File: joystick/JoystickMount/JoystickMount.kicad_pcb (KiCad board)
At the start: 2 copper layers, 2 parts

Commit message: update joystick mount
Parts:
- JOYSTICK_J1: footprint ErgoCai.pretty:CONN-TH_S5B-ZR-LF-SN -> ErgoCai.pretty:FPC-SMD_AFC01-S05FCA-00
- moved JOYSTICK_J1 3.71 mm to (-1.28, 0.00)

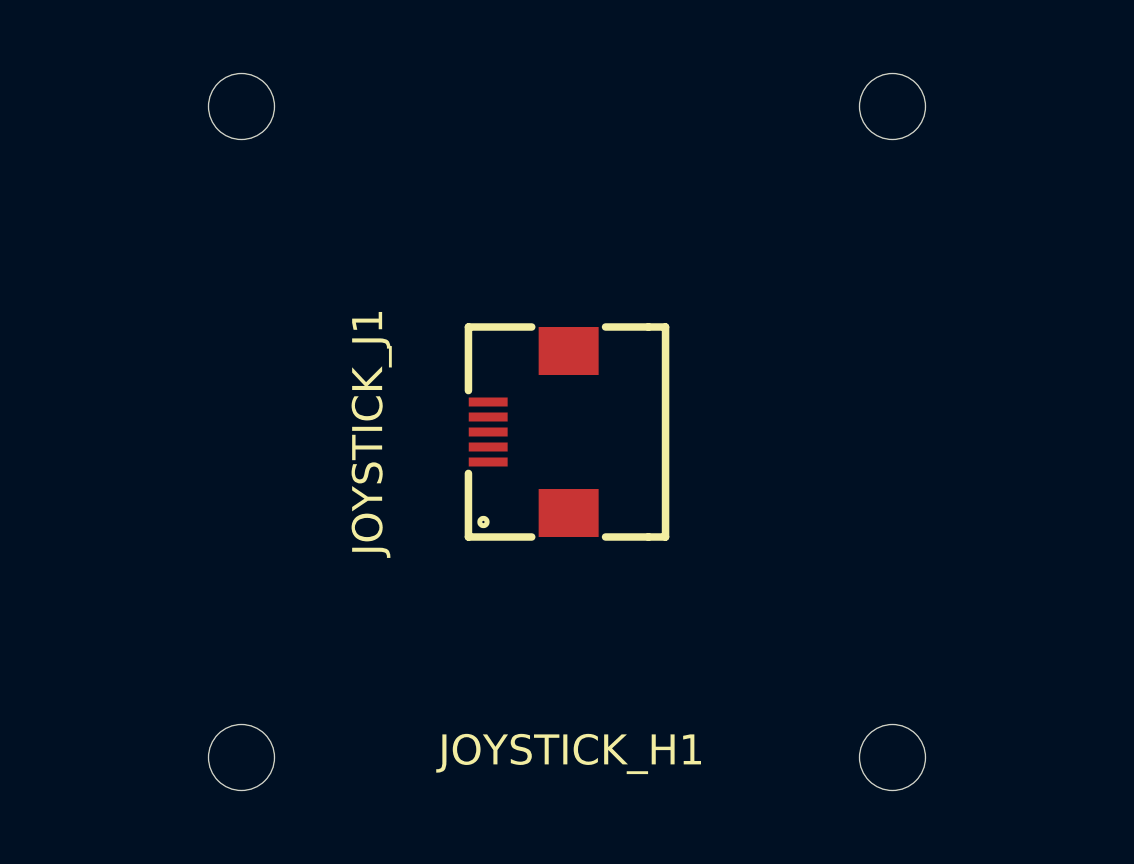
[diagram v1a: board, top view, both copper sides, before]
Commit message: update joystick size
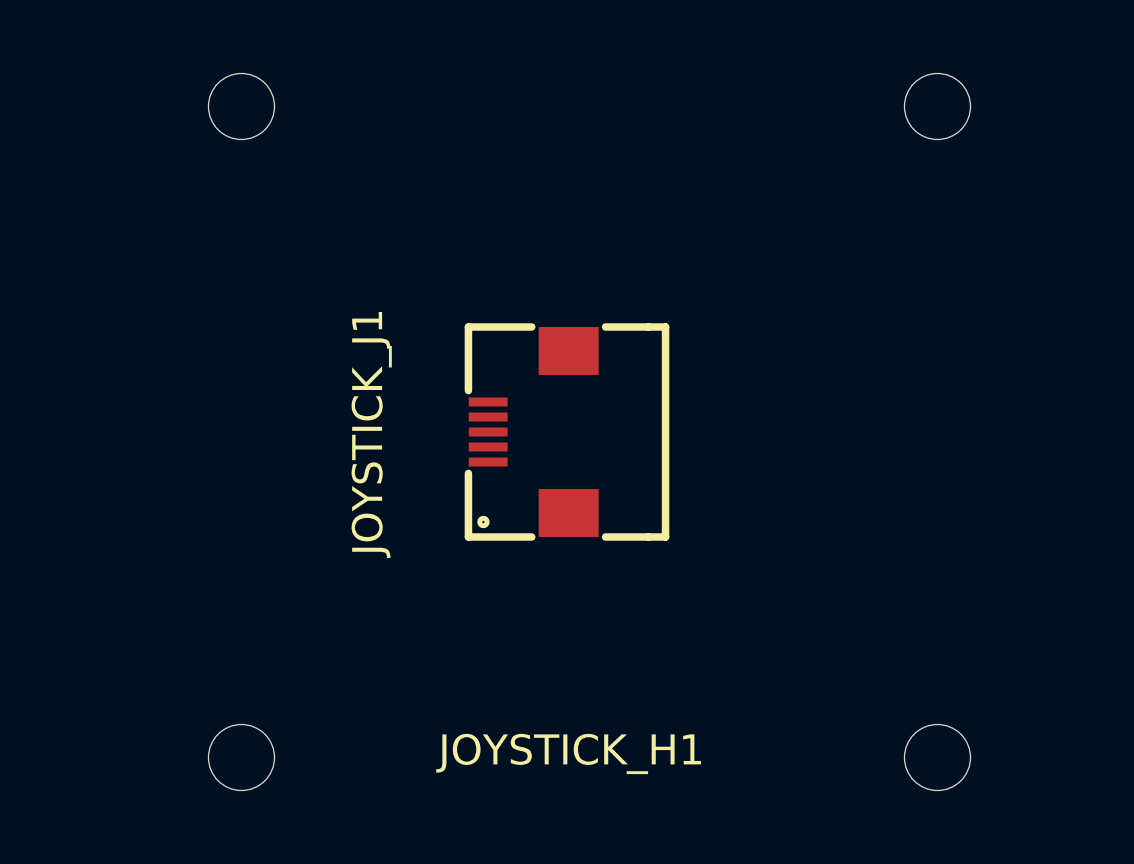
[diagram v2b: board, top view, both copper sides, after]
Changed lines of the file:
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@@
 		(fp_rect
 			(start -13 -13)
-			(end 13 13)
+			(end 14.5 13)
 			(stroke
 				(width 0.1)
@@
 		)
 		(fp_circle
-			(center 10.85 -10.85)
-			(end 12.75 -10.85)
+			(center 12.35 -10.85)
+			(end 14.25 -10.85)
 			(stroke
 				(width 0.15)
@@
 		)
 		(fp_circle
-			(center 10.85 10.85)
-			(end 12.75 10.85)
+			(center 12.35 10.85)
+			(end 14.25 10.85)
 			(stroke
 				(width 0.15)
@@
 		)
 		(fp_circle
-			(center 10.85 -10.85)
-			(end 13 -10.85)
+			(center 12.35 -10.85)
+			(end 14.5 -10.85)
 			(stroke
 				(width 0.05)
@@
 		)
 		(fp_circle
-			(center 10.85 10.85)
-			(end 13 10.85)
+			(center 12.35 10.85)
+			(end 14.5 10.85)
 			(stroke
 				(width 0.05)
@@
 		)
 		(pad "" np_thru_hole circle
-			(at 10.85 -10.85)
+			(at 12.35 -10.85)
 			(size 2.2 2.2)
 			(drill 2.2)
@@
 		)
 		(pad "" np_thru_hole circle
-			(at 10.85 10.85)
+			(at 12.35 10.85)
 			(size 2.2 2.2)
 			(drill 2.2)
@@
 		)
 		(embedded_fonts no)
+		(model "/Users/jinsongc/Development/ErgoCai.modules/joystick/Alpsalpine/Alpsalpine.step"
+			(opacity 0.8100)
+			(offset
+				(xyz 0 0 3.5)
+			)
+			(scale
+				(xyz 1 1 1)
+			)
+			(rotate
+				(xyz -0 -0 -90)
+			)
+		)
+		(model "/Users/jinsongc/Development/ErgoCaiLib/3dmodels/Joystick Cap.stp"
+			(opacity 0.7600)
+			(offset
+				(xyz 0 2.5 23.5)
+			)
+			(scale
+				(xyz 1 1 1)
+			)
+			(rotate
+				(xyz -0 180 90)
+			)
+		)
 	)
 	(embedded_fonts no)

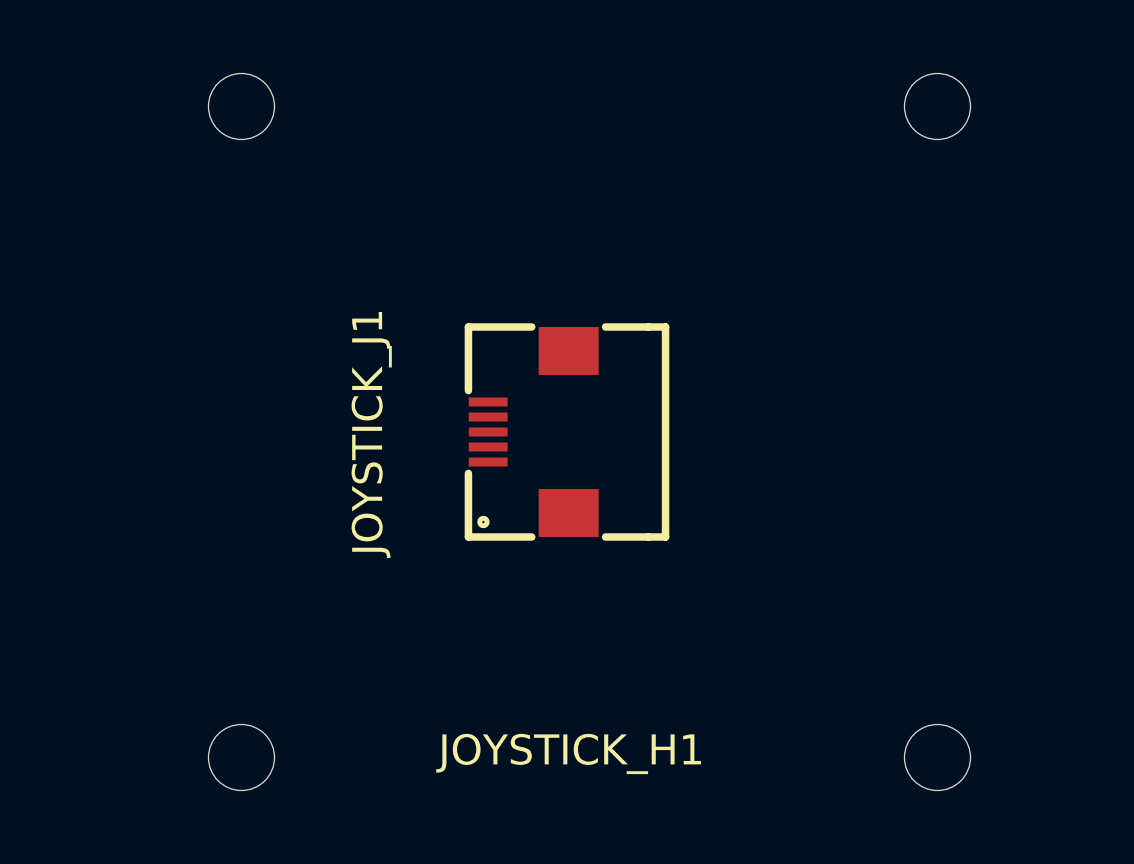
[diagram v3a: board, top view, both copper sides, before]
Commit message: update joystick FPC to 6 pins
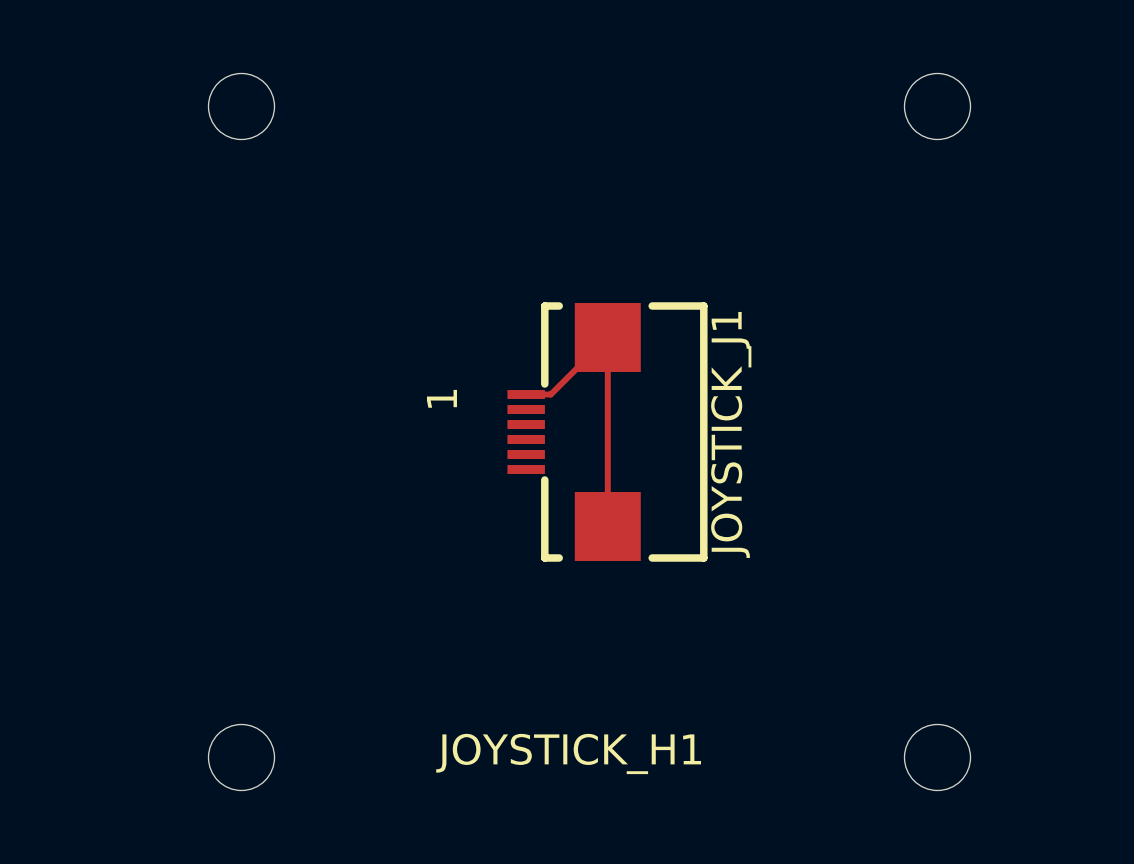
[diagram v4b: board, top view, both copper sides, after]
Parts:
- JOYSTICK_J1: value Conn_01x05 -> AFD01-S06FCA-00; footprint ErgoCai.pretty:FPC-SMD_AFC01-S05FCA-00 -> ErgoCai.pretty:FPC-SMD_6P-P0.50_JS_AFD01-S06FCA-00
- moved JOYSTICK_J1 1.28 mm to (0.00, 0.00), turned to -90 degrees
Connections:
- JOYSTICK_J1 pad 6: (no net) -> unconnected-(JOYSTICK_J1-Pad6)
- JOYSTICK_J1 pad 7: (no net) -> GND
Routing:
- net GND: track 0.00 -> 9.81 mm
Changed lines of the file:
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@@
 	(net 4 "ADC_JT1")
 	(net 5 "ADC_JT2")
-	(footprint "ErgoCai.pretty:FPC-SMD_AFC01-S05FCA-00"
+	(net 6 "unconnected-(JOYSTICK_J1-Pad6)")
+	(footprint "ErgoCai.pretty:FPC-SMD_6P-P0.50_JS_AFD01-S06FCA-00"
 		(layer "F.Cu")
-		(at -1.285 0 90)
+		(at 0 0 -90)
 		(property "Reference" "JOYSTICK_J1"
-			(at 0 -5.34 90)
-			(layer "F.SilkS")
-			(effects
-				(font
-					(size 1 1)
-					(thickness 0.15)
-				)
-			)
-		)
-		(property "Value" "Conn_01x05"
-			(at 0 5.34 90)
-			(layer "F.Fab")
-			(effects
-				(font
-					(size 1 1)
-					(thickness 0.15)
-				)
-			)
-		)
-		(property "Datasheet" "~"
+			(at 0 -5.36 90)
+			(layer "F.SilkS")
+			(effects
+				(font
+					(size 1 1)
+					(thickness 0.15)
+				)
+			)
+		)
+		(property "Value" "AFD01-S06FCA-00"
+			(at 0 5.36 90)
+			(layer "F.Fab")
+			(effects
+				(font
+					(size 1 1)
+					(thickness 0.15)
+				)
+			)
+		)
+		(property "Datasheet" ""
 			(at 0 0 90)
 			(layer "F.Fab")
@@
 			)
 		)
-		(property "Description" "Generic connector, single row, 01x05, script generated (kicad-library-utils/schlib/autogen/connector/)"
+		(property "Description" ""
 			(at 0 0 90)
 			(layer "F.Fab")
@@
 			)
 		)
-		(property ki_fp_filters "Connector*:*_1x??_*")
+		(property "LCSC Part" "C18198574"
+			(at 0 0 270)
+			(unlocked yes)
+			(layer "F.Fab")
+			(hide yes)
+			(effects
+				(font
+					(size 1 1)
+					(thickness 0.15)
+				)
+			)
+		)
 		(sheetname "/")
 		(sheetfile "JoystickMount.kicad_sch")
-		(attr smd)
-		(fp_line
-			(start 3.5 -2)
-			(end 3.5 0.11)
-			(stroke
-				(width 0.25)
-				(type solid)
-			)
-			(layer "F.SilkS")
-		)
-		(fp_line
-			(start 1.38 -2)
-			(end 3.5 -2)
-			(stroke
-				(width 0.25)
-				(type solid)
-			)
-			(layer "F.SilkS")
-		)
-		(fp_line
-			(start -3.5 -2)
-			(end -1.38 -2)
-			(stroke
-				(width 0.25)
-				(type solid)
-			)
-			(layer "F.SilkS")
-		)
-		(fp_line
-			(start -3.5 -2)
-			(end -3.5 0.11)
-			(stroke
-				(width 0.25)
-				(type solid)
-			)
-			(layer "F.SilkS")
-		)
-		(fp_line
-			(start 3.5 2.57)
-			(end 3.5 4)
-			(stroke
-				(width 0.25)
-				(type solid)
-			)
-			(layer "F.SilkS")
-		)
-		(fp_line
-			(start -3.5 2.57)
-			(end -3.5 4)
-			(stroke
-				(width 0.25)
-				(type solid)
-			)
-			(layer "F.SilkS")
-		)
-		(fp_line
-			(start 3.5 4)
-			(end 3.5 4.57)
-			(stroke
-				(width 0.25)
-				(type solid)
-			)
-			(layer "F.SilkS")
-		)
-		(fp_line
-			(start -3.5 4)
-			(end -3.5 4.57)
-			(stroke
-				(width 0.25)
-				(type solid)
-			)
-			(layer "F.SilkS")
-		)
-		(fp_line
-			(start 3.5 4.57)
-			(end -3.5 4.57)
-			(stroke
-				(width 0.25)
-				(type solid)
-			)
-			(layer "F.SilkS")
-		)
-		(fp_circle
-			(center -3 -1.5)
-			(end -2.92 -1.5)
-			(stroke
-				(width 0.25)
-				(type solid)
-			)
-			(fill no)
-			(layer "F.SilkS")
-		)
-		(fp_circle
-			(center -3.45 -1.71)
-			(end -3.42 -1.71)
-			(stroke
-				(width 0.06)
-				(type solid)
-			)
-			(fill no)
-			(layer "F.Fab")
+		(attr through_hole)
+		(fp_line
+			(start -4.2 0.74)
+			(end -1.6 0.74)
+			(stroke
+				(width 0.25)
+				(type solid)
+			)
+			(layer "F.SilkS")
+		)
+		(fp_line
+			(start 4.2 0.74)
+			(end 1.6 0.74)
+			(stroke
+				(width 0.25)
+				(type solid)
+			)
+			(layer "F.SilkS")
+		)
+		(fp_line
+			(start -4.2 0.26)
+			(end -4.2 0.74)
+			(stroke
+				(width 0.25)
+				(type solid)
+			)
+			(layer "F.SilkS")
+		)
+		(fp_line
+			(start 4.2 0.26)
+			(end 4.2 0.74)
+			(stroke
+				(width 0.25)
+				(type solid)
+			)
+			(layer "F.SilkS")
+		)
+		(fp_line
+			(start -4.2 -4.56)
+			(end -4.2 -2.84)
+			(stroke
+				(width 0.25)
+				(type solid)
+			)
+			(layer "F.SilkS")
+		)
+		(fp_line
+			(start 4.2 -4.56)
+			(end 4.2 -2.84)
+			(stroke
+				(width 0.25)
+				(type solid)
+			)
+			(layer "F.SilkS")
+		)
+		(fp_line
+			(start 4.2 -4.56)
+			(end -4.2 -4.56)
+			(stroke
+				(width 0.25)
+				(type solid)
+			)
+			(layer "F.SilkS")
+		)
+		(fp_text user "1"
+			(at -1.53 4.13 90)
+			(layer "F.SilkS")
+			(effects
+				(font
+					(size 1 1)
+					(thickness 0.2)
+				)
+				(justify right)
+			)
 		)
 		(fp_text user "${REFERENCE}"
@@
 		)
 		(pad "1" smd rect
-			(at -1 -1.34 90)
-			(size 0.3 1.3)
+			(at -1.25 1.36 270)
+			(size 0.3 1.25)
 			(layers "F.Cu" "F.Mask" "F.Paste")
 			(net 1 "GND")
-			(pinfunction "Pin_1")
-			(pintype "passive")
+			(pinfunction "1")
+			(pintype "unspecified")
 		)
 		(pad "2" smd rect
-			(at -0.5 -1.34 90)
-			(size 0.3 1.3)
+			(at -0.75 1.36 270)
+			(size 0.3 1.25)
 			(layers "F.Cu" "F.Mask" "F.Paste")
 			(net 2 "3.3V")
-			(pinfunction "Pin_2")
-			(pintype "passive")
+			(pinfunction "2")
+			(pintype "unspecified")
 		)
 		(pad "3" smd rect
-			(at 0 -1.34 90)
-			(size 0.3 1.3)
+			(at -0.25 1.36 270)
+			(size 0.3 1.25)
 			(layers "F.Cu" "F.Mask" "F.Paste")
 			(net 3 "ADC_JT3")
-			(pinfunction "Pin_3")
-			(pintype "passive")
+			(pinfunction "3")
+			(pintype "unspecified")
 		)
 		(pad "4" smd rect
-			(at 0.5 -1.34 90)
-			(size 0.3 1.3)
+			(at 0.25 1.36 270)
+			(size 0.3 1.25)
 			(layers "F.Cu" "F.Mask" "F.Paste")
 			(net 5 "ADC_JT2")
-			(pinfunction "Pin_4")
-			(pintype "passive")
+			(pinfunction "4")
+			(pintype "unspecified")
 		)
 		(pad "5" smd rect
-			(at 1 -1.34 90)
-			(size 0.3 1.3)
+			(at 0.75 1.36 270)
+			(size 0.3 1.25)
 			(layers "F.Cu" "F.Mask" "F.Paste")
 			(net 4 "ADC_JT1")
-			(pinfunction "Pin_5")
-			(pintype "passive")
+			(pinfunction "5")
+			(pintype "unspecified")
 		)
 		(pad "6" smd rect
-			(at 2.7 1.34 90)
-			(size 1.6 2)
-			(layers "F.Cu" "F.Mask" "F.Paste")
+			(at 1.25 1.36 270)
+			(size 0.3 1.25)
+			(layers "F.Cu" "F.Mask" "F.Paste")
+			(net 6 "unconnected-(JOYSTICK_J1-Pad6)")
+			(pinfunction "6")
+			(pintype "unspecified")
 		)
 		(pad "7" smd rect
-			(at -2.7 1.34 90)
-			(size 1.6 2)
-			(layers "F.Cu" "F.Mask" "F.Paste")
+			(at 3.15 -1.36 270)
+			(size 2.3 2.2)
+			(layers "F.Cu" "F.Mask" "F.Paste")
+			(net 1 "GND")
+			(pinfunction "7")
+			(pintype "unspecified")
+		)
+		(pad "8" smd rect
+			(at -3.15 -1.36 270)
+			(size 2.3 2.2)
+			(layers "F.Cu" "F.Mask" "F.Paste")
+			(net 1 "GND")
+			(pinfunction "8")
+			(pintype "unspecified")
 		)
 		(embedded_fonts no)
-		(model "${EASYEDA2KICAD}/easyeda2kicad.3dshapes/FPC-SMD_AFC01-S05FCA-00.wrl"
+		(model "${EASYEDA2KICAD}/easyeda2kicad.3dshapes/FPC-SMD_6P-P0.50_JS_AFD01-S06FCA-00.wrl"
 			(offset
-				(xyz 0 -1.32 -0)
+				(xyz -0 1.53 0)
 			)
 			(scale
@@
 			)
 			(rotate
-				(xyz 0 0 0)
-			)
-		)
-		(model "/Users/jinsongc/Documents/KiCad/easyeda2kicad/easyeda2kicad.3dshapes/FPC-SMD_AFC01-S05FCA-00.step"
-			(offset
-				(xyz 0 -1 2)
-			)
-			(scale
-				(xyz 1 1 1)
-			)
-			(rotate
-				(xyz -0 -0 -0)
+				(xyz 0 0 180)
 			)
 		)
@@
 			)
 		)
-		(property "Datasheet" "~"
+		(property "Datasheet" ""
 			(at 0 0 0)
 			(unlocked yes)
@@
 		)
 	)
+	(segment
+		(start 1.36 -3.15)
+		(end 1.36 3.15)
+		(width 0.2)
+		(layer "F.Cu")
+		(net 1)
+	)
+	(segment
+		(start -1.36 -1.25)
+		(end -0.54 -1.25)
+		(width 0.2)
+		(layer "F.Cu")
+		(net 1)
+	)
+	(segment
+		(start -0.54 -1.25)
+		(end 1.36 -3.15)
+		(width 0.2)
+		(layer "F.Cu")
+		(net 1)
+	)
 	(embedded_fonts no)

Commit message: add joystick_fpc_hole
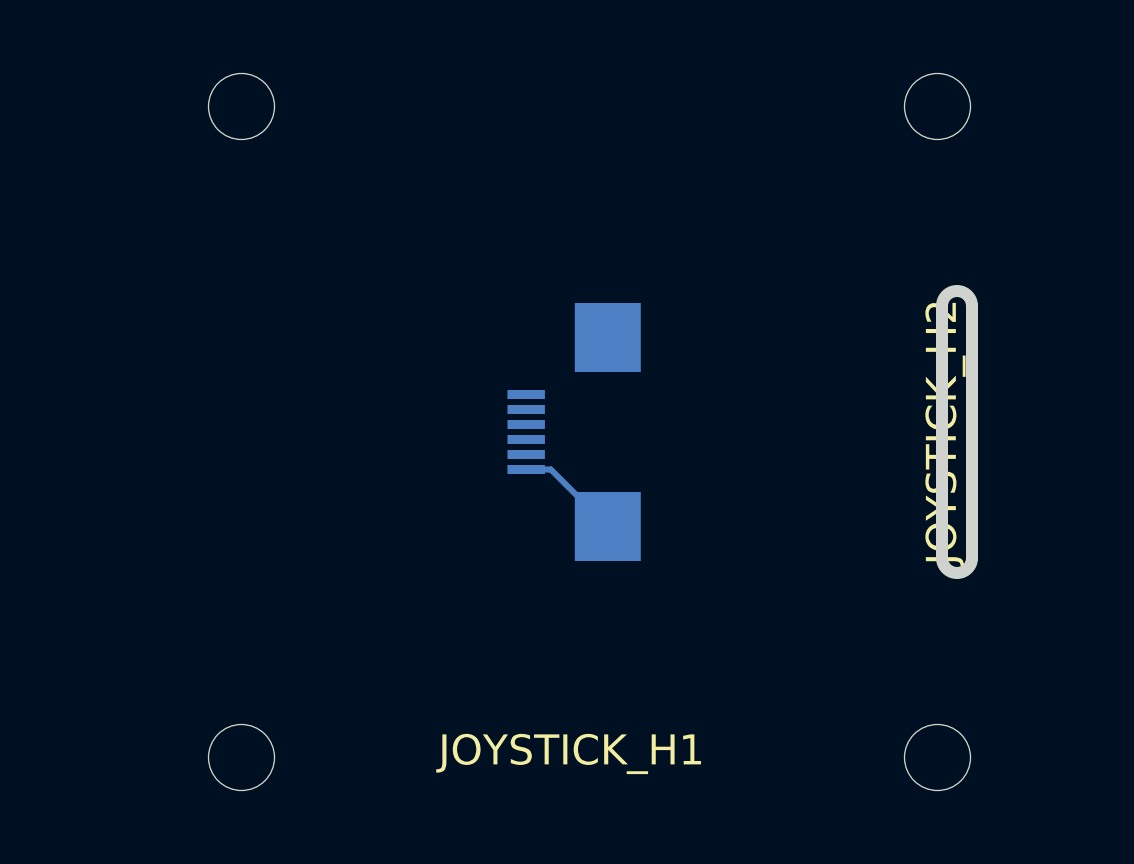
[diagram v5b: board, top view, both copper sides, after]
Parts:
- added JOYSTICK_H2: MountingHole, ErgoCai.pretty:joystick_fpc_hole, F.Cu at (13.0, 0.00)
- JOYSTICK_J1: moved to B.Cu
- turned JOYSTICK_J1 to 90 degrees
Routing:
- net GND: track 9.81 -> 3.51 mm
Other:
- board outline added: 1 x 9.4 mm
